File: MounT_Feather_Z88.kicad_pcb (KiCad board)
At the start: 2 copper layers, 50.8 x 22.9 mm, 10 parts, among them J1 Adafruit_Feather, J2 DE9_Male, U1 MAX3232

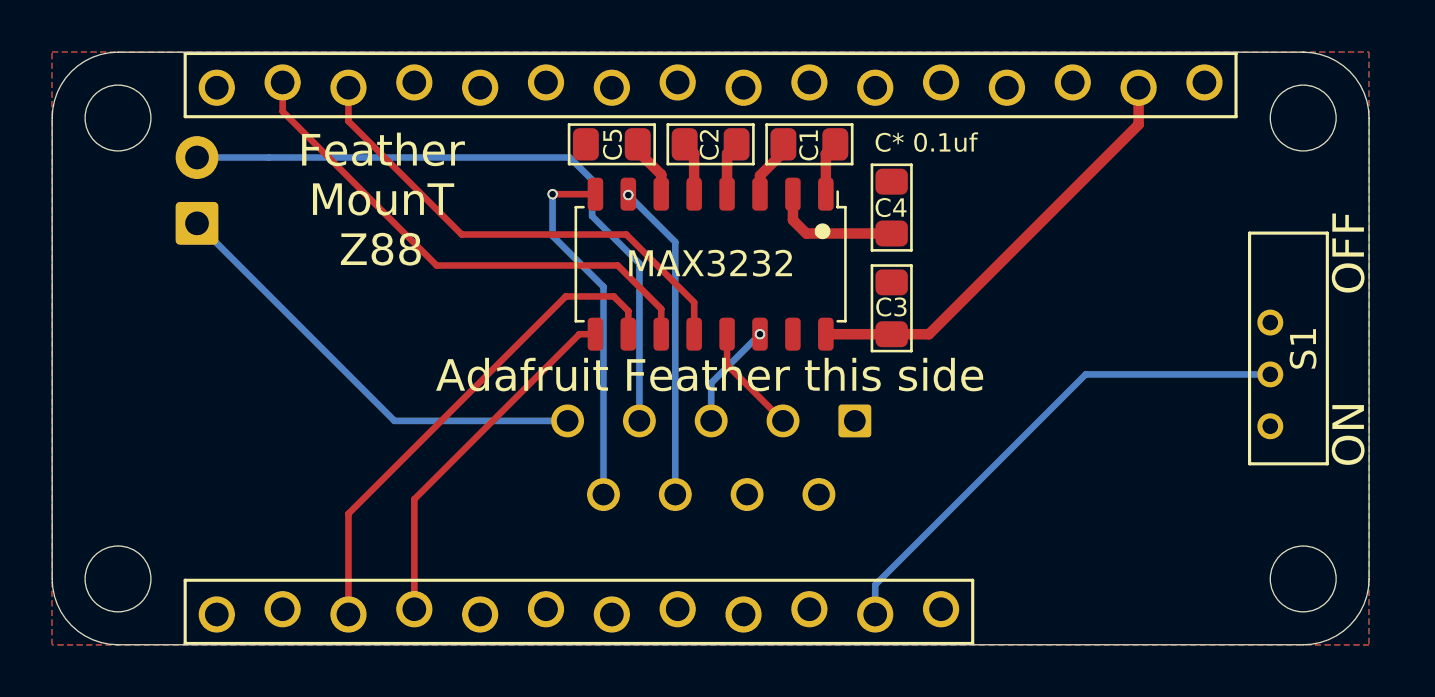
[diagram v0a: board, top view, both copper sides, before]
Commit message: reduce pin stagger offset to 4mil
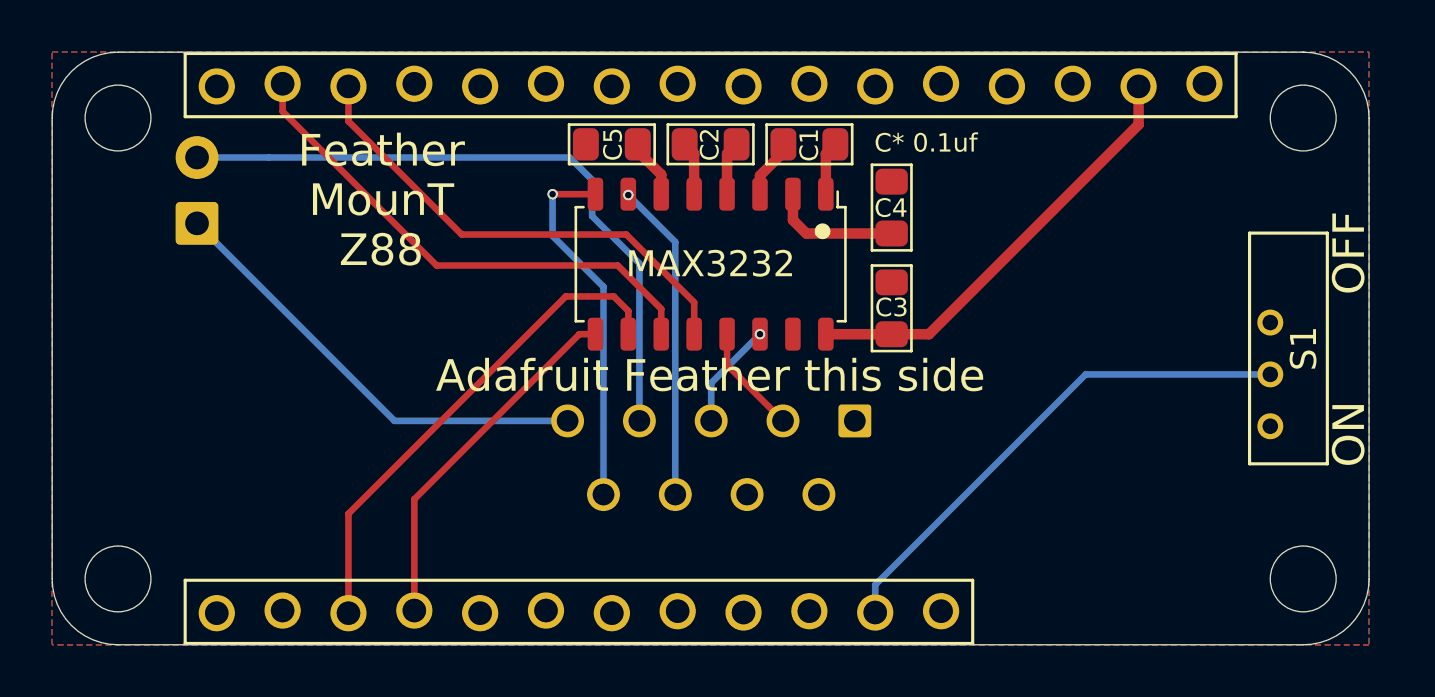
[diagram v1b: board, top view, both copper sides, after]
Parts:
- J1: footprint 0_LOCAL:Adafruit_Feather_stagger -> 0_LOCAL:Adafruit_Feather_stagger_4mil
